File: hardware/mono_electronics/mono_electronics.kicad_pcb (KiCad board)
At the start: 4 copper layers, 190 x 148 mm, 181 parts, among them SW1 KMR2, U1 ESP32-S3FN8, Y1 L327S400H11L

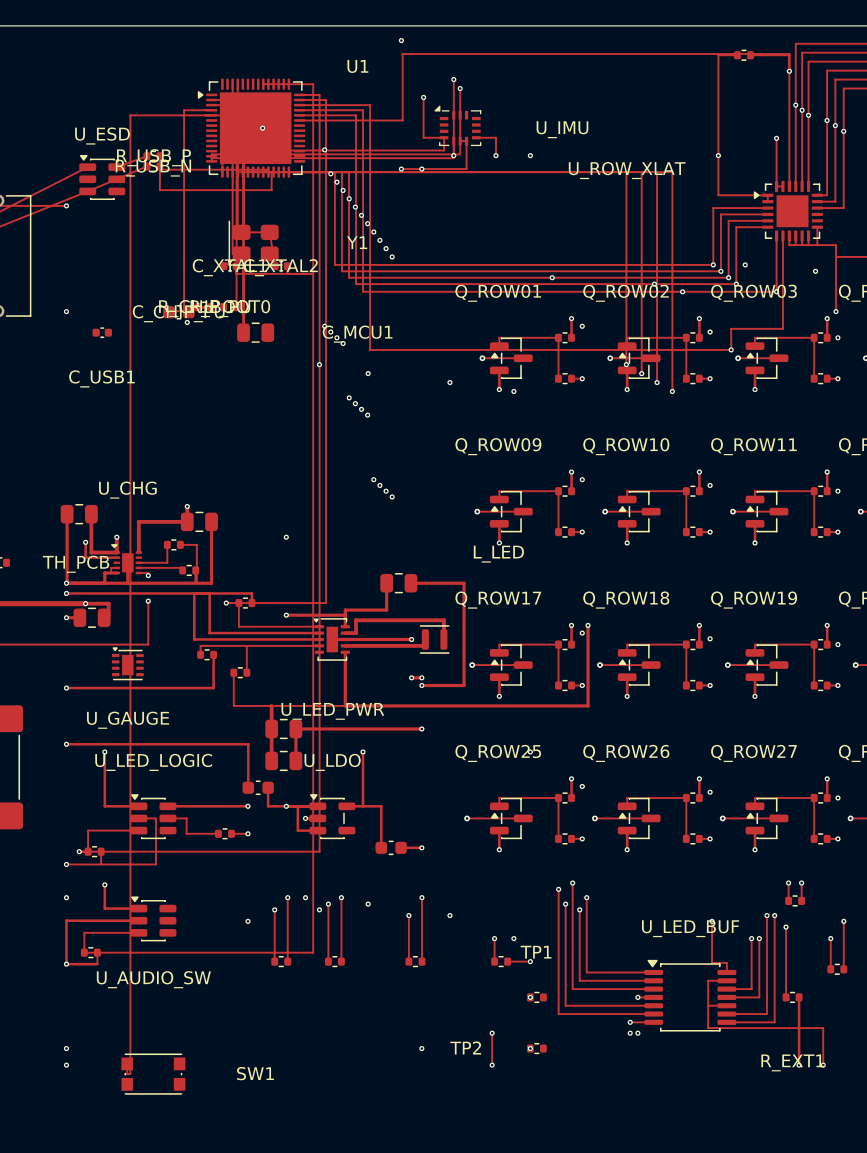
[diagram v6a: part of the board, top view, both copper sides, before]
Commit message: Improve mono electronics MCU escape DRC and GPIO documentation
Route row/decoder GPIOs on dedicated pad columns, enables on In2 spines,
and fix the EVT pin table (no GPIO19/20 vs row overlap). Electronics
DRC violations drop 316→277; panels stay clean.

Co-authored-by: illiapliukhin <illiapliukhin@users.noreply.github.com>
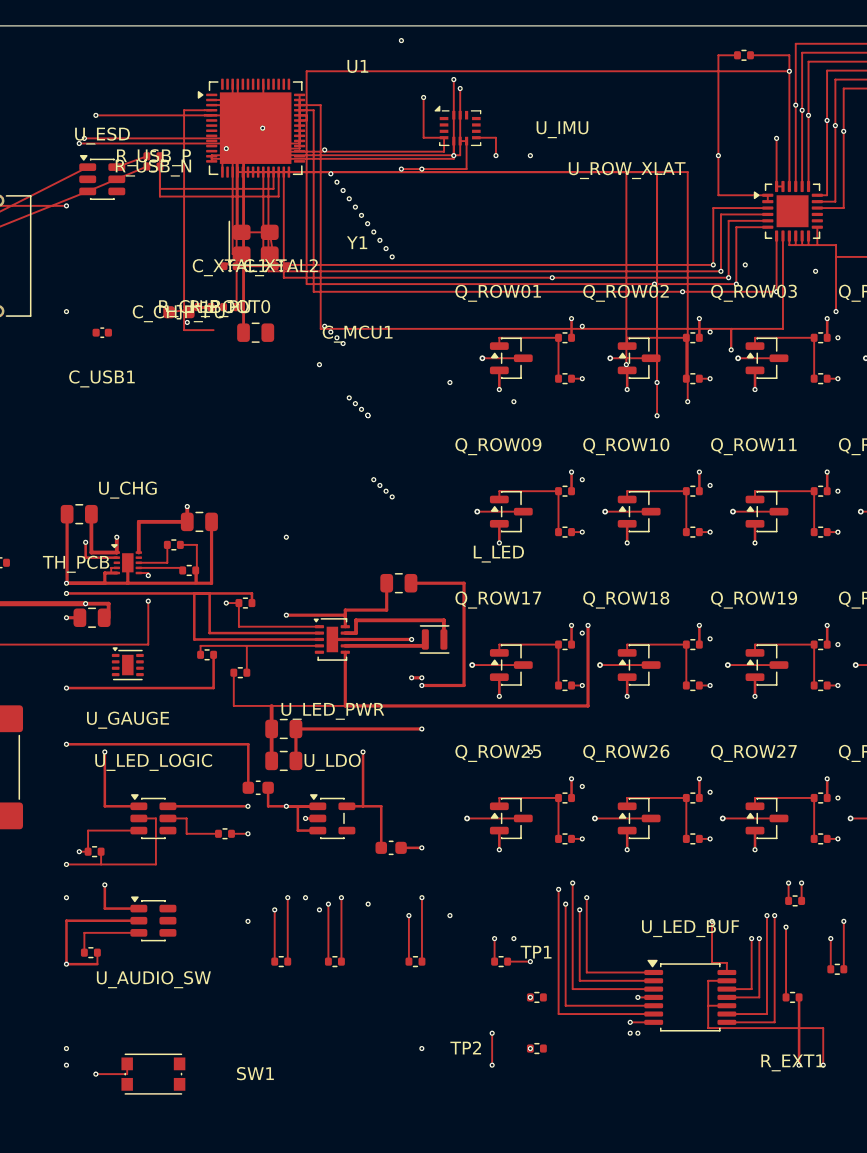
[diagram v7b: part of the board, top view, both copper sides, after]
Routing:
- net AUDIO_EN: track 95.5 -> 87.8 mm, vias 0 -> 1
- net GPIO0_BOOT: track 99.9 -> 104.8 mm, vias 0 -> 2
- net AON_3V3: track 215.5 -> 219.7 mm
- net LED_EN: track 256.4 -> 252.3 mm, vias 3 -> 4
- net LED_LOGIC_EN: track 285.7 -> 282.5 mm, vias 3 -> 4
- net ROW_XLAT_OE_N: track 200.9 -> 198.2 mm
- net USB_D_N_MCU: track 9.33 -> 12.0 mm
- net LED_SDI: track 215.7 -> 218.1 mm
- net LED_OE_N: track 206.3 -> 208.7 mm
- net USB_D_P_MCU: track 13.4 -> 14.4 mm
- net GND: track 927.2 -> 928.1 mm

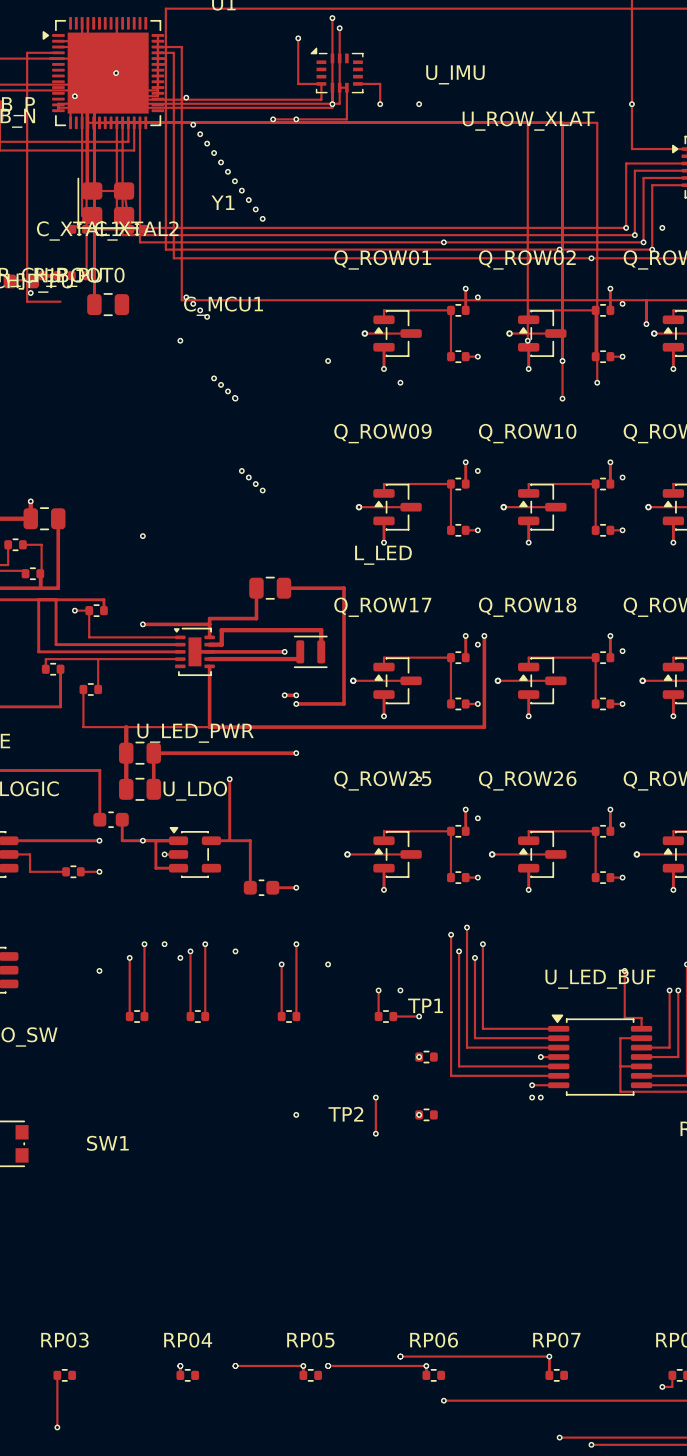
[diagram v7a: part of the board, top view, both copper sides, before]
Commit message: Route MCU LED nets via eastern In2 spine; gate verify on copper
Replace row-fan-in reserve drops for LED_CLK/SDI/LE/OE_N with an In2
eastern path to RP pads so LED_SDI no longer shorts ROW_08_Y.

Electronics verify checks shorting_items and tracks_crossing only;
panels unchanged at 0/0. Document escape rules in MONO_SPLIT_ARCHITECTURE.

Co-authored-by: illiapliukhin <illiapliukhin@users.noreply.github.com>
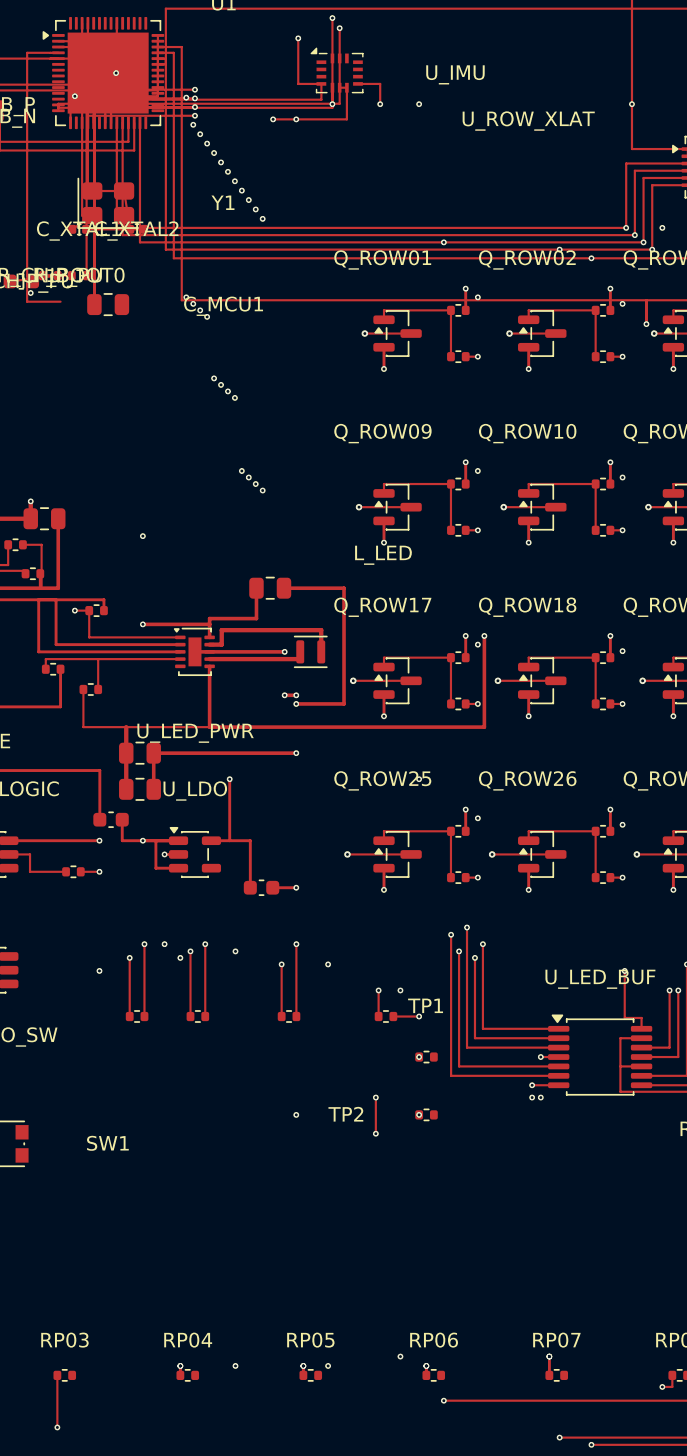
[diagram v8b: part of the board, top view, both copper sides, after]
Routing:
- net LED_CLK: track 209.1 -> 337.0 mm, vias 7 -> 6
- net LED_SDI: track 218.1 -> 334.6 mm, vias 8 -> 7
- net LED_LE: track 218.8 -> 333.8 mm, vias 8 -> 7
- net LED_OE_N: track 208.7 -> 314.6 mm, vias 8 -> 7
